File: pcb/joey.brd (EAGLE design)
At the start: 42.3 x 49.3 mm, 61 parts, among them J1 AVR_SPI_PRG_6PTH, U1 ATMEGA168, U2 TMP102, X1 USB-MICROB, Y1 13.56M

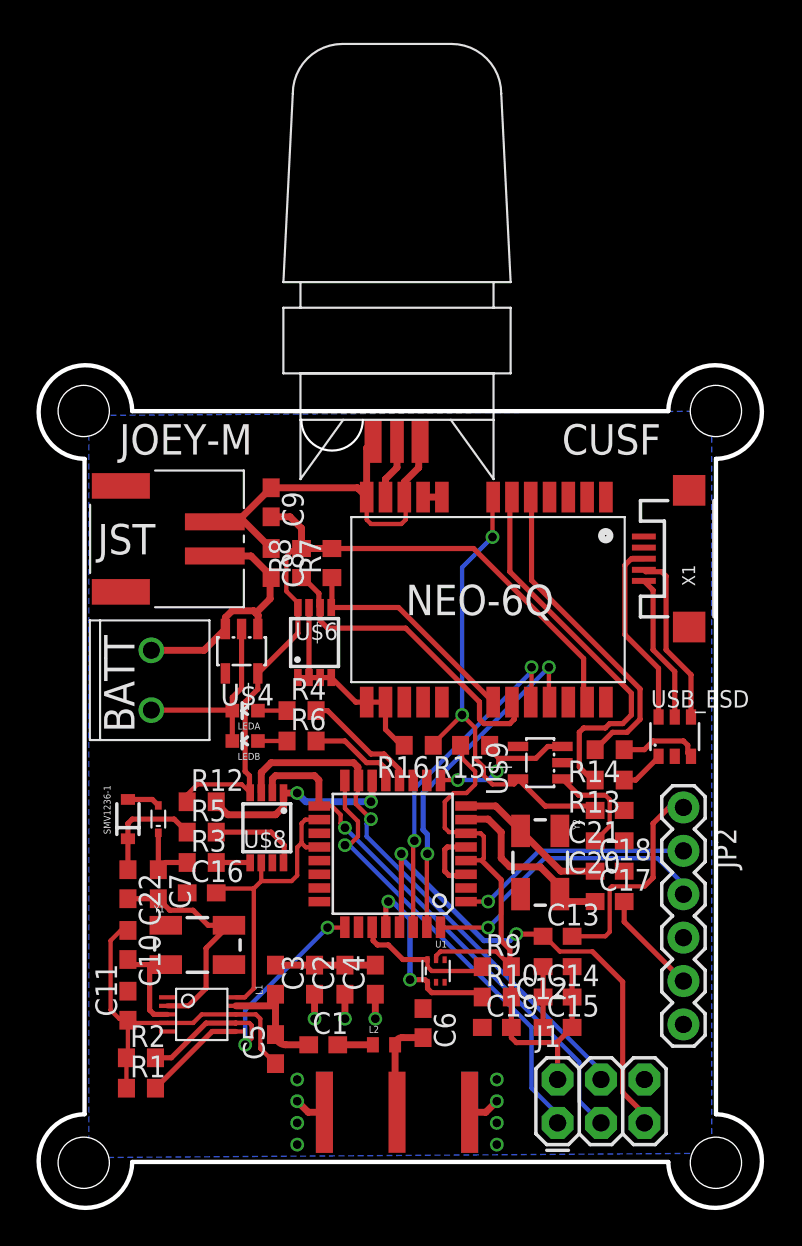
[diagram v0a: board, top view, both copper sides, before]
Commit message: Fixed filter bug in the schematic, almost finished routing
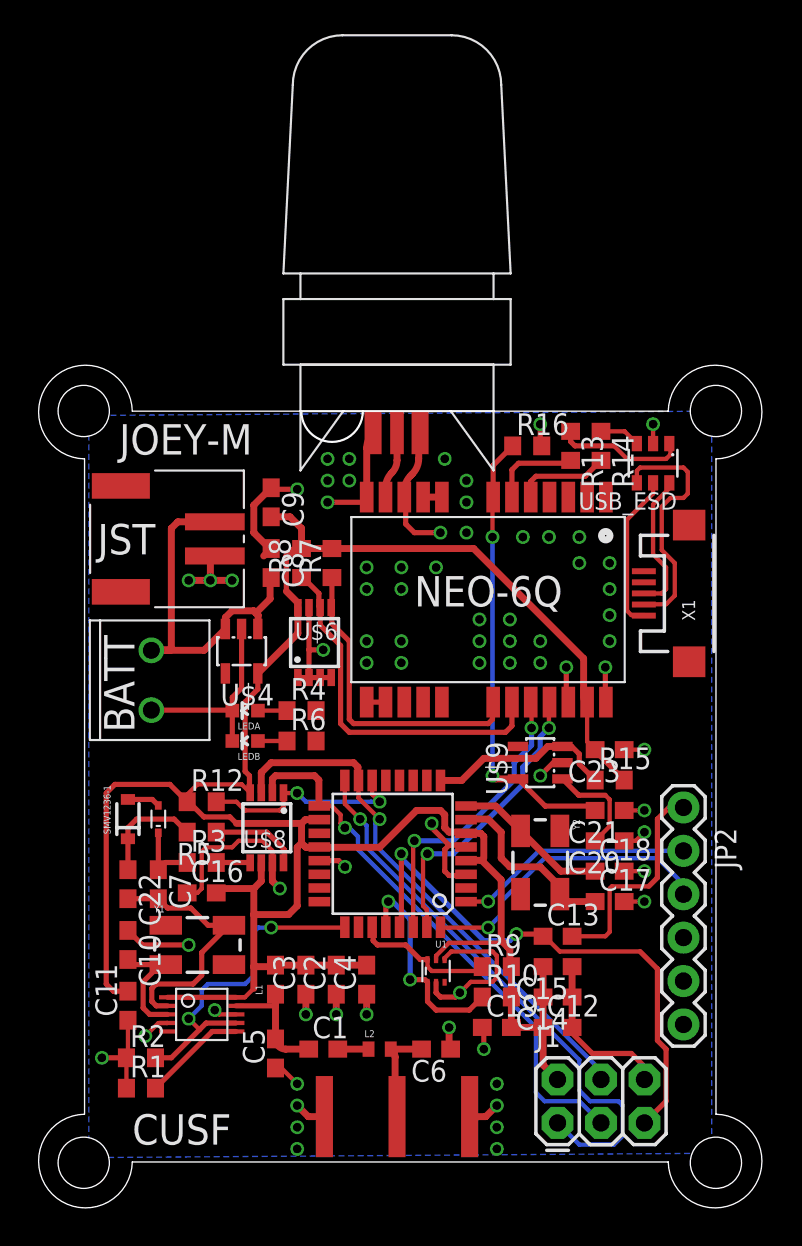
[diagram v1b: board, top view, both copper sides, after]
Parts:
- added C23: 100nF, rcl:C0603
- moved R13 19.7 mm to (31.5, 45.0), turned to 270 degrees
- moved R16 18.6 mm to (29.0, 45.0), turned to 0 degrees
- moved R14 17.8 mm to (33.3, 45.0), turned to 270 degrees
- moved USB_ESD 16.1 mm to (36.3, 43.9), turned to 180 degrees
- moved R15 8.13 mm to (33.8, 25.4), turned to 0 degrees
- moved C12 3.56 mm to (30.7, 10.9), turned to 0 degrees
- moved C15 3.56 mm to (30.7, 14.5), turned to 180 degrees
- moved X1 2.03 mm to (38.4, 36.3)
- moved C6 1.70 mm to (23.6, 9.65), turned to 180 degrees
- moved C3 0.51 mm to (16.0, 13.7)
- moved C2 0.51 mm to (17.8, 13.7)
- moved C4 0.51 mm to (19.6, 13.7)
- moved U$2 0.51 mm to (21.3, 45.7)
- moved L2 0.36 mm to (20.3, 9.65)
- moved C1 0.25 mm to (17.0, 9.65)
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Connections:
- removed net N$4: C2.2, C3.2, C4.2, L1.2
- new net COARSE_V: C22.1, R5.2, SMV1236-1.1
- net COARSE: no longer C22.1, R5.2, SMV1236-1.1
- net DC_IN: now also U$5.VBATT; no longer U$5.V+
- net GND: now also C23.1
- net VCC: now also C2.2, C23.2, C3.2, C4.2, L1.2
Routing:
- net VCC: track 102.8 -> 146.7 mm
- net GND: track 93.0 -> 123.6 mm, vias 11 -> 71
- net N$20: track 22.5 -> 5.26 mm
- net N$21: track 19.2 -> 5.54 mm
- net DC_IN: track 14.7 -> 22.0 mm
- net LEDA: track 6.97 -> 0.00 mm
- net MISO: track 26.1 -> 33.1 mm
- net COARSE: track 11.9 -> 5.19 mm
- net COARSE_V: track 0.00 -> 6.45 mm
- net N$4: track 5.84 -> 0.00 mm
- net LEDB: track 5.37 -> 0.00 mm
- net GPS_DP: track 2.47 -> 7.63 mm
- net GPS_I2C_SDA: track 13.5 -> 18.4 mm
- net N$18: track 10.3 -> 14.5 mm
- net GPS_TX: track 20.4 -> 17.3 mm
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
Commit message: Finished routing for v1.0
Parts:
- moved X1 1.79 mm to (38.6, 34.5)
- moved U$9 1.02 mm to (29.7, 25.4)
- moved LEDA 0.72 mm to (11.9, 29.0)
- moved LEDB 0.72 mm to (11.9, 27.2)
- moved R4 0.72 mm to (15.2, 29.0)
- moved R6 0.72 mm to (15.2, 27.2)
- moved C20 0.51 mm to (33.8, 21.3)
- moved R3 0.51 mm to (9.91, 20.1)
- moved U$8 0.51 mm to (13.7, 22.1)
- moved Y2 0.51 mm to (29.7, 20.1)
- moved C11 0.51 mm to (5.59, 11.7)
- moved C12 0.51 mm to (30.7, 10.4)
- moved C13 0.51 mm to (30.7, 15.7)
- moved C19 0.51 mm to (27.2, 10.4)
- moved R2 0.51 mm to (6.35, 8.64)
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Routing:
- net LEDA: track 0.00 -> 7.51 mm
- net LEDB: track 0.00 -> 5.95 mm
- net VCC: track 146.7 -> 150.0 mm
- net VBUS_3V3: track 26.9 -> 28.5 mm
- net N$16: track 9.32 -> 10.9 mm
- net N$18: track 14.5 -> 16.0 mm
- net N$19: track 8.33 -> 9.75 mm
- net GPS_USB_EN: track 11.0 -> 10.3 mm
- net SCK: track 32.4 -> 31.9 mm
- net MOSI: track 32.0 -> 31.5 mm
- net N$7: track 5.87 -> 5.36 mm
- net GPS_TX: track 17.3 -> 17.8 mm
- net GPS_RX: track 17.5 -> 18.0 mm
- net RESET: track 32.3 -> 31.8 mm
- net MISO: track 33.1 -> 32.5 mm
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- added copper zone on layer 1, net GND
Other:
- board size 42.3 x 49.3 mm -> 42.8 x 49.8 mm
- board text added: "AVR"
- board text added: "BLK"
- board text added: "FTDI"
- board text added: "GRN"
- board text added: "ICSP"
- board text added: "MAR '12"
- board text added: "SMA"
- board text added: "USB"
- board text added: "v1.0"

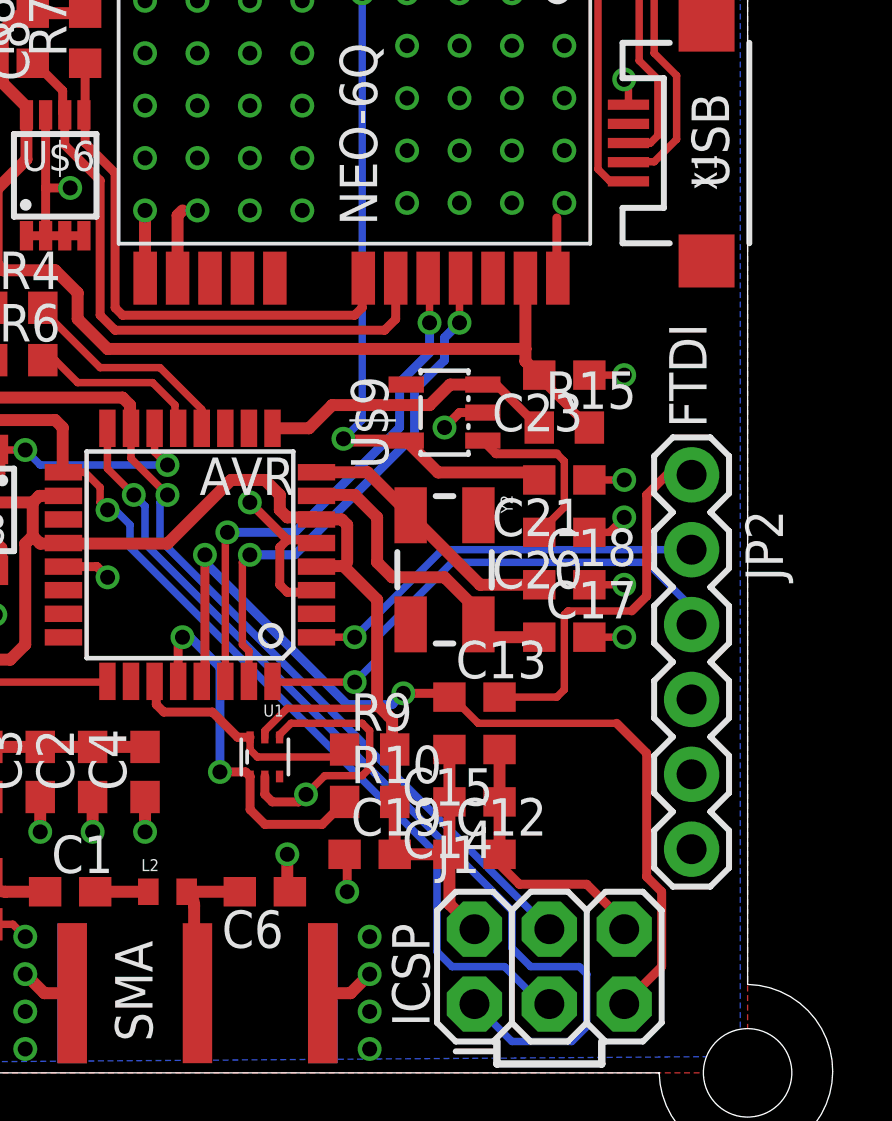
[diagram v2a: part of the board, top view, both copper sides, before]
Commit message: Finished routing, updated completed BOM for v1.0
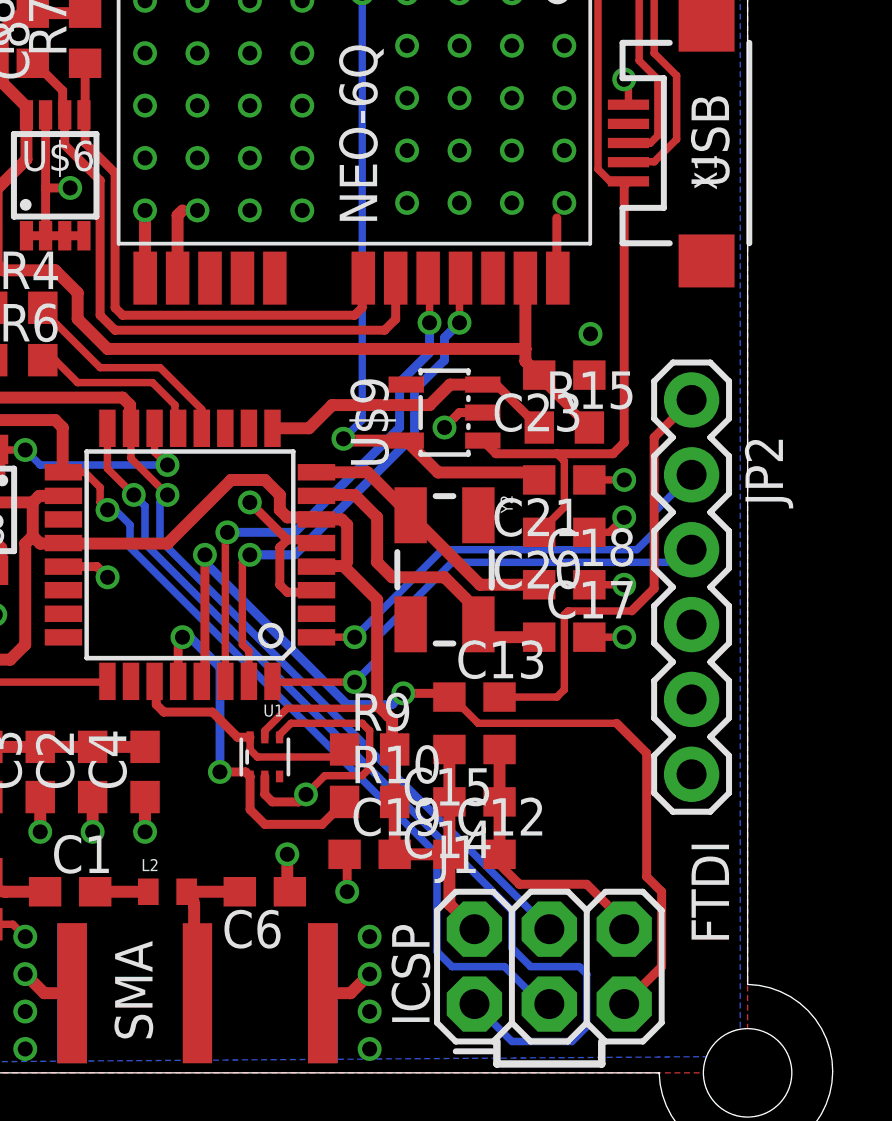
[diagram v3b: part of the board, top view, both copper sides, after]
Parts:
- C22: value 35pF -> 36pF
- moved JP2 2.54 mm to (38.1, 25.8)
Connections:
- removed net N$16: USB_ESD.5, X1.VBUS
- net VBUS: now also USB_ESD.5, X1.VBUS
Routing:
- net VBUS: track 5.82 -> 28.1 mm
- net N$16: track 10.9 -> 0.00 mm
- net N$3: track 13.2 -> 15.2 mm
- net FTDI_TX: track 14.0 -> 15.4 mm
- net GND: track 123.6 -> 122.5 mm
- net FTDI_RX: track 17.6 -> 16.5 mm
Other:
- board text removed: "AVR"
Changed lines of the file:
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@@
 <text x="14.732" y="44.45" size="1.778" layer="22" font="vector" ratio="15" rot="MR0">JOEY-M</text>
 <text x="14.732" y="39.116" size="1.778" layer="22" font="vector" ratio="15" rot="MR0">MAR '12</text>
-<text x="39.37" y="28.448" size="1.27" layer="22" font="vector" ratio="15" rot="MR270">GRN</text>
-<text x="39.37" y="9.398" size="1.27" layer="22" font="vector" ratio="15" rot="MR270">BLK</text>
+<text x="36.068" y="28.702" size="1.27" layer="22" font="vector" ratio="15" rot="MR180">GRN</text>
+<text x="36.068" y="11.43" size="1.27" layer="22" font="vector" ratio="15" rot="MR180">BLK</text>
 <text x="29.21" y="4.572" size="1.27" layer="21" font="vector" ratio="15" rot="R90">ICSP</text>
-<text x="38.608" y="24.892" size="1.27" layer="21" font="vector" ratio="15" rot="R90">FTDI</text>
+<text x="39.37" y="7.366" size="1.27" layer="21" font="vector" ratio="15" rot="R90">FTDI</text>
 <text x="19.812" y="4.064" size="1.27" layer="21" font="vector" ratio="15" rot="R90">SMA</text>
 <text x="4.064" y="38.862" size="1.27" layer="21" font="vector" ratio="15">JST</text>
@@
 <text x="27.432" y="31.75" size="1.27" layer="21" font="vector" ratio="15" rot="R90">NEO-6Q</text>
 <text x="39.37" y="33.02" size="1.27" layer="21" font="vector" ratio="15" rot="R90">USB</text>
-<text x="24.638" y="23.876" size="1.27" layer="21" font="vector" ratio="15" rot="R180">AVR</text>
 </plain>
 <attributes>
@@
 <element name="U1" library="SparkFun" package="TQFP32-08" value="ATMEGA168" x="21.082" y="20.574" rot="R180"/>
 <element name="J1" library="SparkFun" package="2X3" value="AVR_SPI_PRG_6PTH" x="30.734" y="5.334"/>
-<element name="JP2" library="SparkFun" package="FTDI_BASIC" value="FTDI_BASICPTH" x="38.1" y="23.288" rot="R270"/>
+<element name="JP2" library="SparkFun" package="FTDI_BASIC" value="FTDI_BASICPTH" x="38.1" y="25.828" rot="R270"/>
 <element name="C13" library="rcl" package="C0603" value="100n" x="30.734" y="15.748"/>
 <element name="C12" library="rcl" package="C0603" value="100n" x="30.734" y="10.414"/>
@@
 <element name="C17" library="rcl" package="C0603" value="18pF" x="33.782" y="17.78"/>
 <element name="C18" library="rcl" package="C0603" value="18pF" x="33.782" y="19.558"/>
-<element name="C22" library="rcl" package="C0603" value="35pF" x="5.588" y="18.796" rot="R270"/>
+<element name="C22" library="rcl" package="C0603" value="36pF" x="5.588" y="18.796" rot="R270"/>
 <element name="R5" library="rcl" package="R0603" value="1M" x="9.906" y="21.844" rot="R180"/>
 <element name="SMV1236-1" library="SparkFun" package="SOD-323" value="" x="5.588" y="22.606" rot="R90"/>
@@
 <via x="35.814" y="23.114" extent="1-16" drill="0.508"/>
 <wire x1="34.632" y1="23.114" x2="35.814" y2="23.114" width="0.254" layer="1"/>
-<via x="35.814" y="26.67" extent="1-16" drill="0.508"/>
-<wire x1="34.632" y1="26.67" x2="35.814" y2="26.67" width="0.254" layer="1"/>
+<via x="34.671" y="28.067" extent="1-16" drill="0.508"/>
 <via x="36.322" y="46.228" extent="1-16" drill="0.508"/>
 <wire x1="36.322" y1="45.092" x2="36.322" y2="46.228" width="0.254" layer="1"/>
@@
 <contactref element="JP2" pad="DTR"/>
 <contactref element="C13" pad="2"/>
-<wire x1="36.576" y1="22.606" x2="37.338" y2="23.368" width="0.3048" layer="1"/>
-<wire x1="37.338" y1="23.368" x2="38.02" y2="23.368" width="0.3048" layer="1"/>
-<wire x1="38.02" y1="23.368" x2="38.1" y2="23.288" width="0.3048" layer="1"/>
-<wire x1="36.576" y1="22.606" x2="36.576" y2="19.177" width="0.3048" layer="1"/>
-<wire x1="36.576" y1="19.177" x2="36.068" y2="18.669" width="0.3048" layer="1"/>
+<wire x1="36.83" y1="24.558" x2="36.83" y2="19.431" width="0.3048" layer="1"/>
+<wire x1="36.83" y1="19.431" x2="36.068" y2="18.669" width="0.3048" layer="1"/>
 <wire x1="36.068" y1="18.669" x2="33.909" y2="18.669" width="0.254" layer="1"/>
 <wire x1="33.909" y1="18.669" x2="33.782" y2="18.542" width="0.254" layer="1"/>
@@
 <wire x1="33.782" y1="16.002" x2="33.528" y2="15.748" width="0.254" layer="1"/>
 <wire x1="33.528" y1="15.748" x2="31.584" y2="15.748" width="0.254" layer="1"/>
+<wire x1="36.83" y1="24.558" x2="38.1" y2="25.828" width="0.3048" layer="1"/>
 </signal>
 <signal name="N$11">
@@
 <wire x1="27.432" y1="17.018" x2="27.432" y2="17.78" width="0.254" layer="16"/>
 <wire x1="27.432" y1="17.78" x2="29.972" y2="20.32" width="0.254" layer="16"/>
-<wire x1="29.972" y1="20.32" x2="36.576" y2="20.32" width="0.254" layer="16"/>
-<wire x1="36.576" y1="20.32" x2="38.1" y2="18.796" width="0.254" layer="16"/>
-<wire x1="38.1" y1="18.796" x2="38.1" y2="18.208" width="0.254" layer="16"/>
+<wire x1="29.972" y1="20.32" x2="37.672" y2="20.32" width="0.254" layer="16"/>
+<wire x1="37.672" y1="20.32" x2="38.1" y2="20.748" width="0.254" layer="16"/>
 </signal>
 <signal name="FTDI_TX">
 <contactref element="U1" pad="1"/>
 <contactref element="JP2" pad="RXI"/>
-<wire x1="38.1" y1="20.748" x2="29.638" y2="20.748" width="0.254" layer="16"/>
+<wire x1="36.83" y1="21.336" x2="36.242" y2="20.748" width="0.254" layer="16"/>
+<wire x1="36.242" y1="20.748" x2="29.638" y2="20.748" width="0.254" layer="16"/>
 <wire x1="29.638" y1="20.748" x2="26.67" y2="17.78" width="0.254" layer="16"/>
 <via x="26.67" y="17.78" extent="1-16" drill="0.508"/>
 <wire x1="26.67" y1="17.78" x2="25.3806" y2="17.78" width="0.254" layer="1"/>
 <wire x1="25.3806" y1="17.78" x2="25.3746" y2="17.774" width="0.254" layer="1"/>
+<wire x1="36.83" y1="21.336" x2="36.83" y2="22.018" width="0.254" layer="16"/>
+<wire x1="36.83" y1="22.018" x2="38.1" y2="23.288" width="0.254" layer="16"/>
 </signal>
 <signal name="DC_IN">
@@
 <wire x1="33.782" y1="23.749" x2="33.782" y2="22.186" width="0.254" layer="1"/>
 <wire x1="33.782" y1="22.186" x2="32.932" y2="21.336" width="0.254" layer="1"/>
-</signal>
-<signal name="N$16">
 <contactref element="X1" pad="VBUS"/>
 <contactref element="USB_ESD" pad="5"/>
@@
 <wire x1="34.925" y1="33.655" x2="35.336" y2="33.244" width="0.254" layer="1"/>
 <wire x1="35.336" y1="33.244" x2="35.958" y2="33.244" width="0.254" layer="1"/>
+<wire x1="33.528" y1="24.003" x2="35.433" y2="24.003" width="0.3048" layer="1"/>
+<wire x1="35.433" y1="24.003" x2="35.814" y2="24.384" width="0.3048" layer="1"/>
+<wire x1="35.814" y1="24.384" x2="35.814" y2="33.1" width="0.3048" layer="1"/>
+<wire x1="35.814" y1="33.1" x2="35.958" y2="33.244" width="0.3048" layer="1"/>
 </signal>
 <signal name="N$18">
@@
 </signal>
 </signals>
-<errors>
-</errors>
 </board>
 </drawing>
